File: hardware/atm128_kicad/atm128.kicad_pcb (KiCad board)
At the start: 2 copper layers, 76.2 x 55.9 mm, 58 parts, among them J1 Power Jack, J2 Conn_02x16_Odd_Even, J3 Conn_02x16_Odd_Even, J4 ISP, J5 JTAG, J6 USB_B_Mini, U1 LM2596S-5, U2 ATmega128-16A, U3 CH340G, Y1 Crystal

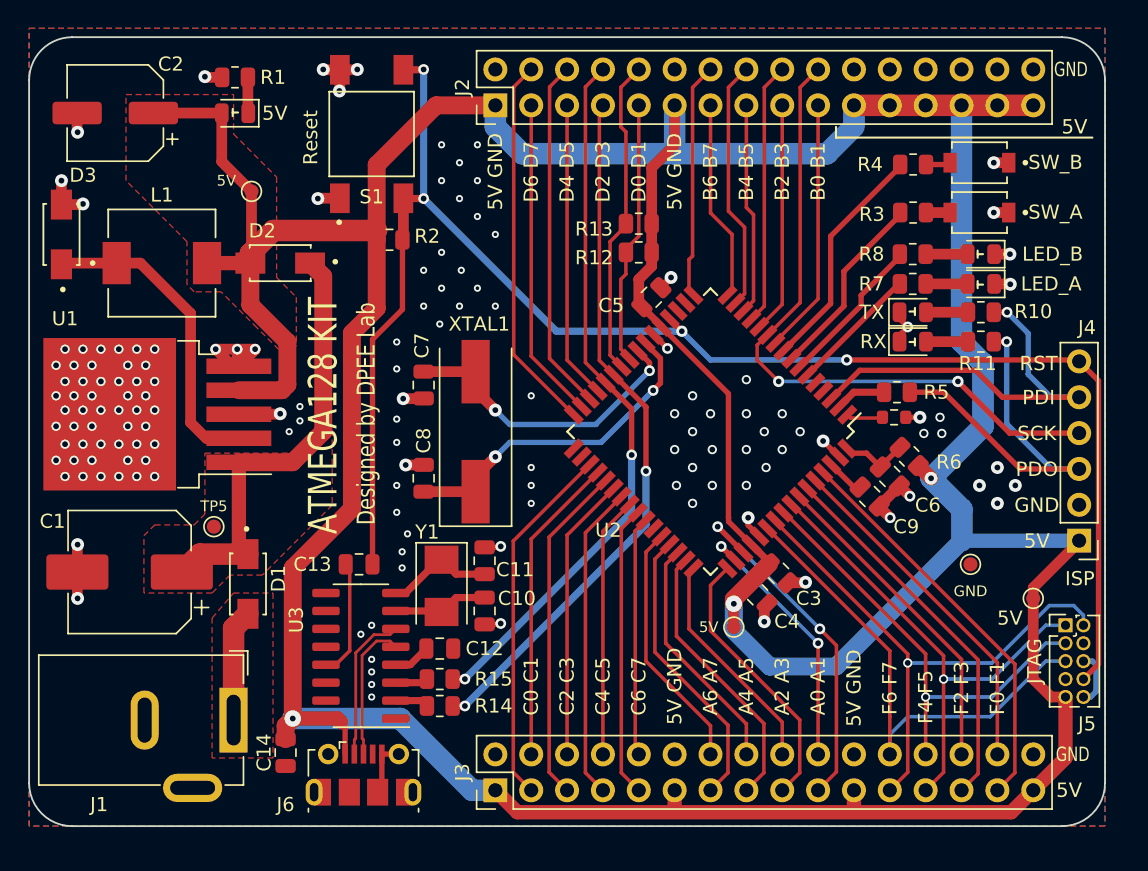
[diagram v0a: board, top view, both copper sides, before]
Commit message: feat: update hw: USB_C, IDC ISP, CH340E
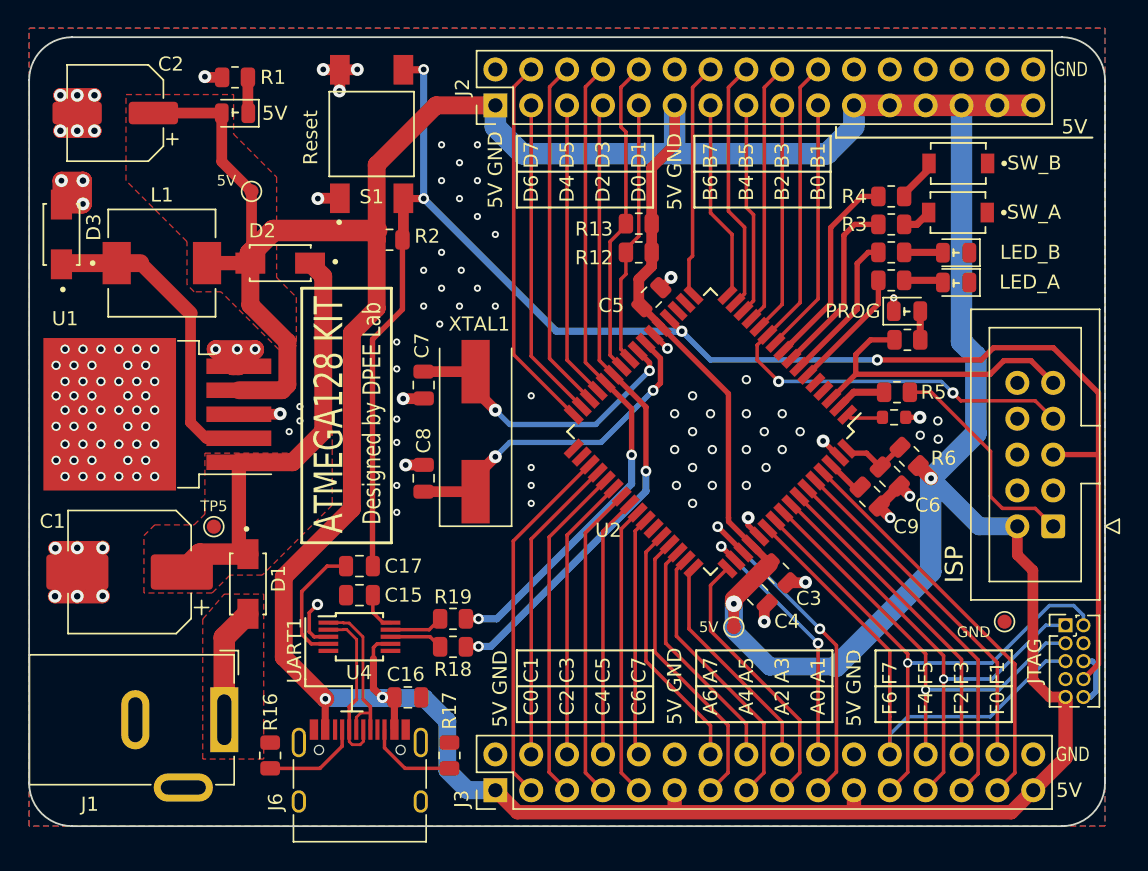
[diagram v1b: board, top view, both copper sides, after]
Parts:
- removed C10, C11, C14: 1uF, Capacitor_SMD:C_0805_2012Metric
- removed C12: 10nF, Capacitor_SMD:C_0805_2012Metric
- removed C13: 100nF, Capacitor_SMD:C_0805_2012Metric
- removed D8: RX, LED_SMD:LED_0805_2012Metric
- removed R11, R14, R15: 1k, Resistor_SMD:R_0805_2012Metric
- removed TP3: 5V, TestPoint:TestPoint_Pad_D1.0mm
- removed U3: CH340G, Package_SO:SOIC-16_3.9x9.9mm_P1.27mm
- removed Y1: Crystal, Crystal:Crystal_SMD_5032-2Pin_5.0x3.2mm
- added C15: 10nF, Capacitor_SMD:C_0805_2012Metric, F.Cu at (76.7, 64.9)
- added C16: 1uF, Capacitor_SMD:C_0805_2012Metric, F.Cu at (80.2, 72.2)
- added C17: 100nF, Capacitor_SMD:C_0805_2012Metric, F.Cu at (76.7, 62.9)
- added R16: 5.1k, Resistor_SMD:R_0805_2012Metric, F.Cu at (70.4, 76.3)
- added R17: 5.1k, Resistor_SMD:R_0805_2012Metric, F.Cu at (83.1, 76.3)
- added R18: 1k, Resistor_SMD:R_0805_2012Metric, F.Cu at (83.4, 68.6)
- added R19: 1k, Resistor_SMD:R_0805_2012Metric, F.Cu at (83.4, 66.6)
- added U4: CH340E, Package_SO:MSOP-10_3x3mm_P0.5mm, F.Cu at (76.7, 67.9)
- D7: value TX -> PROG
- J4: footprint Connector_PinHeader_2.54mm:PinHeader_1x06_P2.54mm_Vertical -> Connector_IDC:IDC-Header_2x05_P2.54mm_Vertical
- J6: value USB_B_Mini -> USB_C_Receptacle_USB2.0; footprint Connector_USB:USB_Micro-B_Molex-105017-0001 -> Connector_USB:USB_C_Receptacle_HRO_TYPE-C-31-M-12
- moved R10 5.56 mm to (115.5, 46.8), turned to 0 degrees
- moved TP4 4.73 mm to (122.4, 66.8)
- moved R4 2.74 mm to (114.4, 36.7)
- moved J4 2.10 mm to (125.9, 60.0)
- moved R3 1.76 mm to (114.4, 38.7)
- moved D6 1.76 mm to (119.0, 40.7)
- moved D5 1.76 mm to (119.0, 42.8)
- moved R7 1.55 mm to (114.4, 42.6)
- moved R8 1.53 mm to (114.4, 40.6)
- moved S2 1.52 mm to (119.1, 37.8)
- moved S3 1.50 mm to (119.2, 34.3)
- moved J6 0.89 mm to (76.8, 78.5)
- moved J1 0.66 mm to (67.2, 73.7)
- moved D7 0.41 mm to (115.5, 44.8)
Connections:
- J4 pad 1: +5V -> /RXD0
- J4 pad 2: GND -> +5V
- J4 pad 3: /RXD0 -> unconnected-(J4-Pad3)
- J4 pad 4: /SPI_SCK -> GND
- J4 pad 5: /TXD0 -> /nRST
- J4 pad 6: //reset -> GND
- J5 pad 8: //reset -> /nRST
- R2 pad 2: //reset -> /nRST
- S1 pad 3: //reset -> /nRST
- S1 pad 4: //reset -> /nRST
- U2 pad 20: //reset -> /nRST
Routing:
- net /nRST: track 0.00 -> 118.4 mm, vias 0 -> 4
- net //reset: track 114.8 -> 0.00 mm, vias 4 -> 0
- net GND: track 59.4 -> 85.3 mm, vias 147 -> 139
- net /RXD0: track 27.4 -> 16.0 mm, vias 1 -> 0
- net Net-(C17-Pad1): track 0.00 -> 9.08 mm
- net Net-(C13-Pad1): track 8.34 -> 0.00 mm
- net Net-(C11-Pad2): track 7.69 -> 0.00 mm
- net /TXD0: track 29.4 -> 22.1 mm, vias 1 -> 0
- net Net-(J6-PadA5): track 0.00 -> 6.93 mm
- net Net-(C10-Pad2): track 6.74 -> 0.00 mm
- net Net-(J6-PadB5): track 0.00 -> 6.50 mm
- net /RXD1: track 50.2 -> 46.1 mm
- net /TXD1: track 50.8 -> 46.9 mm
- net Net-(D8-Pad2): track 2.98 -> 0.00 mm
- net /USB_D+: track 10.0 -> 12.8 mm
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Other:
- board text added: "LED_A PE4 LED_B PE5 SW_A PE6 SW_B PE7"
- board text added: "MISO"
- board text added: "MOSI"
- board text added: "Rev1.0"
- board text added: "UART1"
- board text removed: "PDI"
- board text removed: "PDO"
- board text removed: "Prototype Rev0.0"

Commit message: feat: modify J2, J3 space to 2000mils
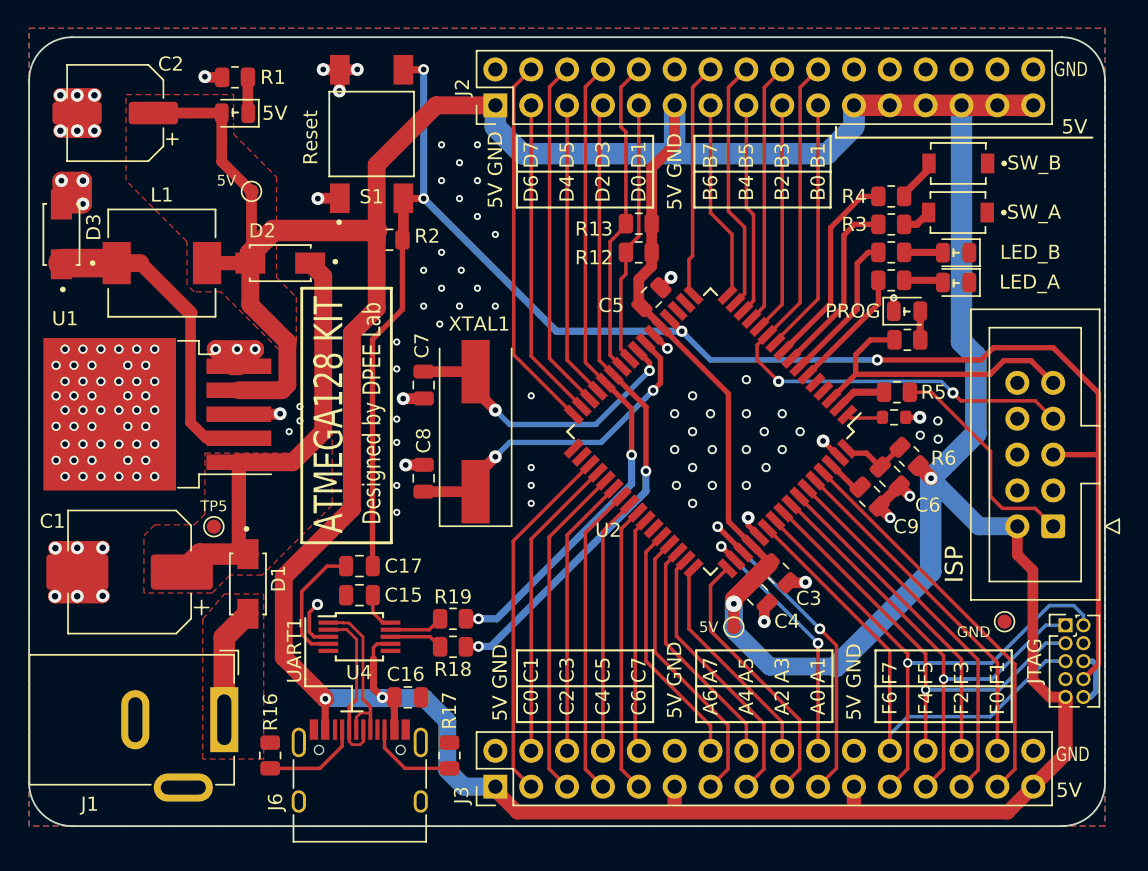
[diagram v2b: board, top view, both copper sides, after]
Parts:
- moved J3 0.25 mm to (86.4, 78.5)

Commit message: feat: update schematic Rev1.0
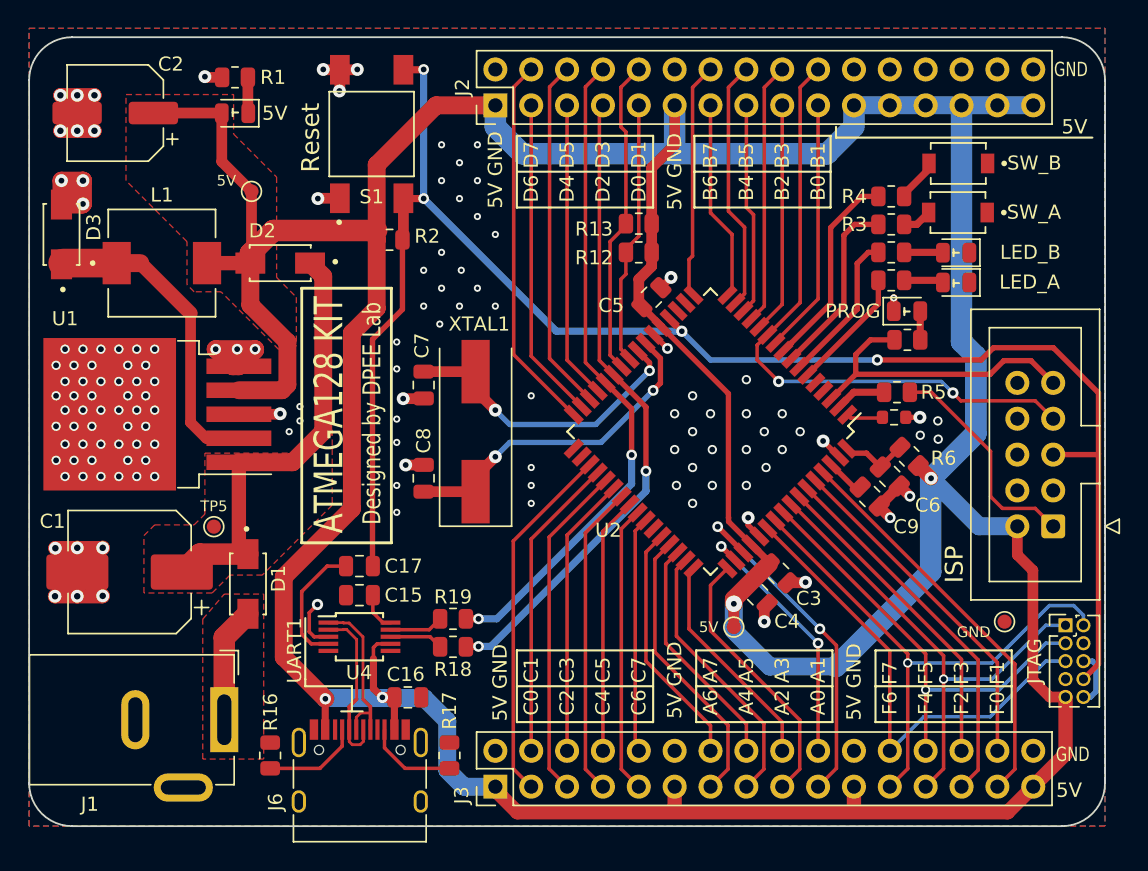
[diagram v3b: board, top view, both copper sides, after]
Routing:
- net /jtag_TDI: track 35.3 -> 34.4 mm
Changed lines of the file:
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@@
     )
     (fp_text value "Reset" (at -0.254 -4.318 90) (layer "F.SilkS")
-      (effects (font (size 1 1) (thickness 0.15)))
+      (effects (font (size 1.27 1.27) (thickness 0.15)))
     )
     (fp_line (start 3 3) (end -3 3) (layer "F.SilkS") (width 0.127))
@@
   (segment (start 99.06 33.02) (end 99.06 30.226) (width 0.762) (layer "F.Cu") (net 3))
   (segment (start 77.9545 39.751) (end 77.9545 39.0925) (width 1.27) (layer "F.Cu") (net 3))
-  (segment (start 111.76 30.226) (end 124.46 30.226) (width 1.524) (layer "F.Cu") (net 3))
   (via (at 74.3204 72.263) (size 0.8) (drill 0.4) (layers "F.Cu" "B.Cu") (net 3))
   (via (at 117.221 56.642) (size 0.9144) (drill 0.4064) (layers "F.Cu" "B.Cu") (net 3))
@@
   (segment (start 84.1248 78.486) (end 86.36 78.486) (width 1.27) (layer "B.Cu") (net 3))
   (segment (start 82.9564 77.3176) (end 84.1248 78.486) (width 1.27) (layer "B.Cu") (net 3))
+  (segment (start 111.76 30.226) (end 124.46 30.226) (width 1.27) (layer "B.Cu") (net 3))
   (segment (start 78.3082 72.2122) (end 74.3712 72.2122) (width 1.27) (layer "B.Cu") (net 3))
   (segment (start 120.6246 60.0456) (end 117.221 56.642) (width 1.27) (layer "B.Cu") (net 3))
@@
   (segment (start 114.299989 75.945989) (end 114.3 75.946) (width 0.254) (layer "F.Cu") (net 20))
   (segment (start 105.630509 60.198936) (end 114.299989 68.868416) (width 0.254) (layer "F.Cu") (net 20))
-  (segment (start 115.569989 73.533011) (end 114.299989 74.803011) (width 0.254) (layer "B.Cu") (net 20))
+  (segment (start 121.411989 73.533011) (end 116.712989 73.533011) (width 0.254) (layer "B.Cu") (net 20))
+  (segment (start 126.746 69.596) (end 125.349 69.596) (width 0.254) (layer "B.Cu") (net 20))
+  (segment (start 116.712989 73.533011) (end 114.299989 75.946011) (width 0.254) (layer "B.Cu") (net 20))
   (segment (start 125.349 69.596) (end 121.411989 73.533011) (width 0.254) (layer "B.Cu") (net 20))
-  (segment (start 126.746 69.596) (end 125.349 69.596) (width 0.254) (layer "B.Cu") (net 20))
-  (segment (start 121.411989 73.533011) (end 115.569989 73.533011) (width 0.254) (layer "B.Cu") (net 20))
-  (segment (start 114.299989 74.803011) (end 114.299989 76.2) (width 0.254) (layer "B.Cu") (net 20))
   (segment (start 111.74791 50.546) (end 113.8955 50.546) (width 0.508) (layer "F.Cu") (net 22))
   (segment (start 110.721677 51.572233) (end 111.74791 50.546) (width 0.508) (layer "F.Cu") (net 22))
